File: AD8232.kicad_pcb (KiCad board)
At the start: 2 copper layers, 33 parts, among them J1 Conn_01x03, J2 Conn_01x06, J3 AudioJack3, M1 AD8232

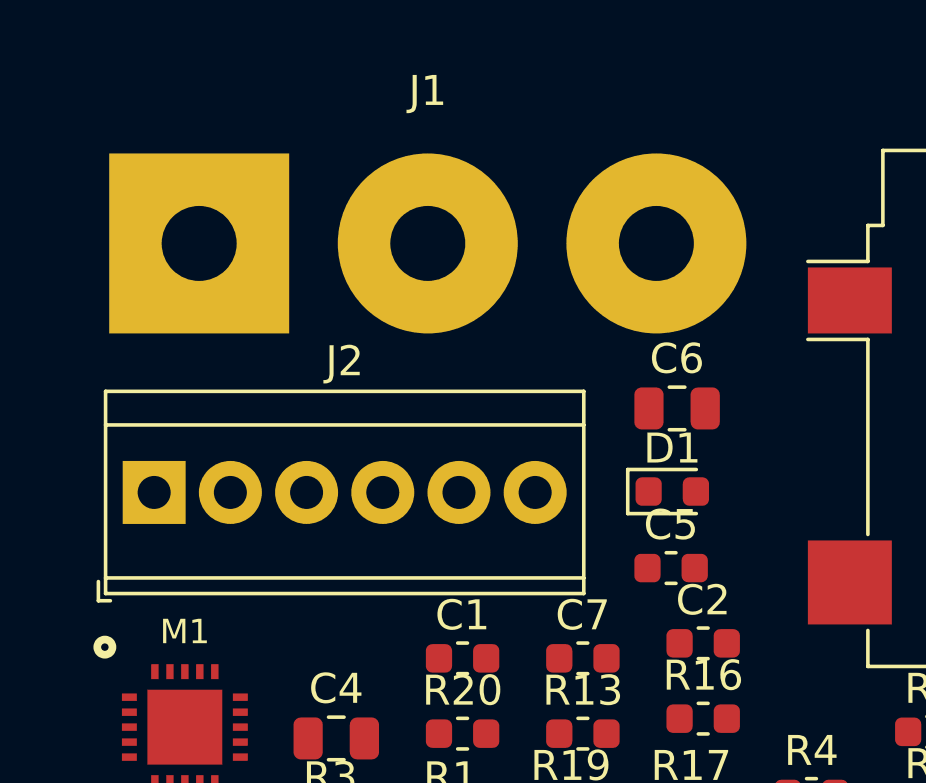
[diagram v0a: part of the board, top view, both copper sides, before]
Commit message: usar huellas de conectores 1x03 y 1x06 de SparkFun
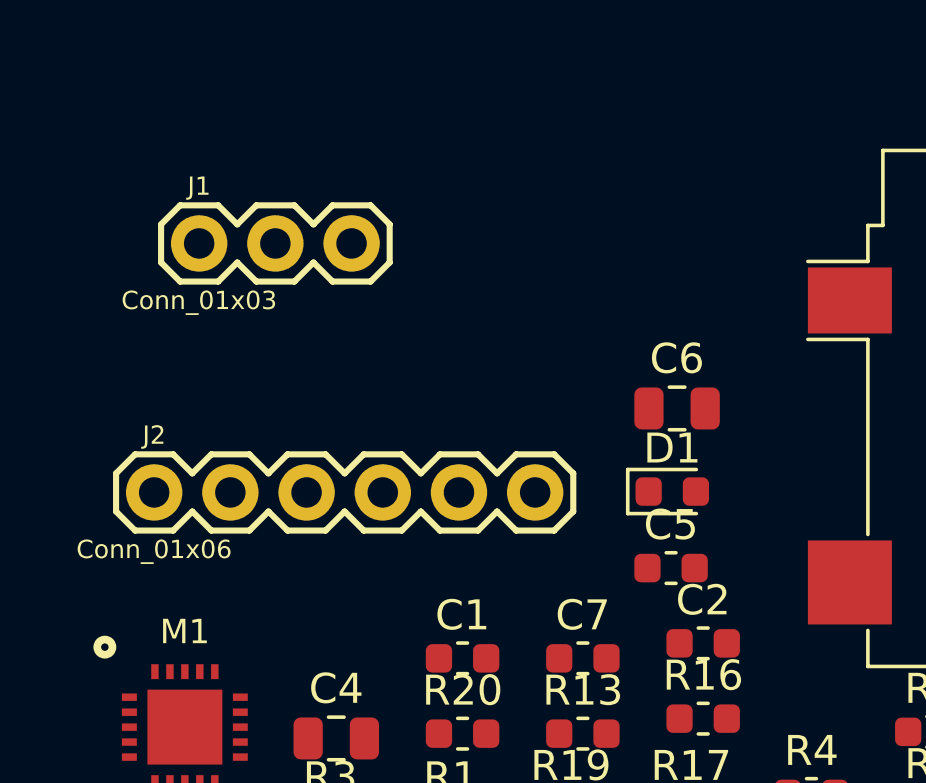
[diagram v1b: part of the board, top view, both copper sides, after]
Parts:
- J1: footprint Connector_Wire:SolderWirePad_1x03_P7.62mm_Drill2.5mm -> fp:1X03
- J2: footprint TerminalBlock_TE-Connectivity:TerminalBlock_TE_282834-6_1x06_P2.54mm_Horizontal -> fp:1X06

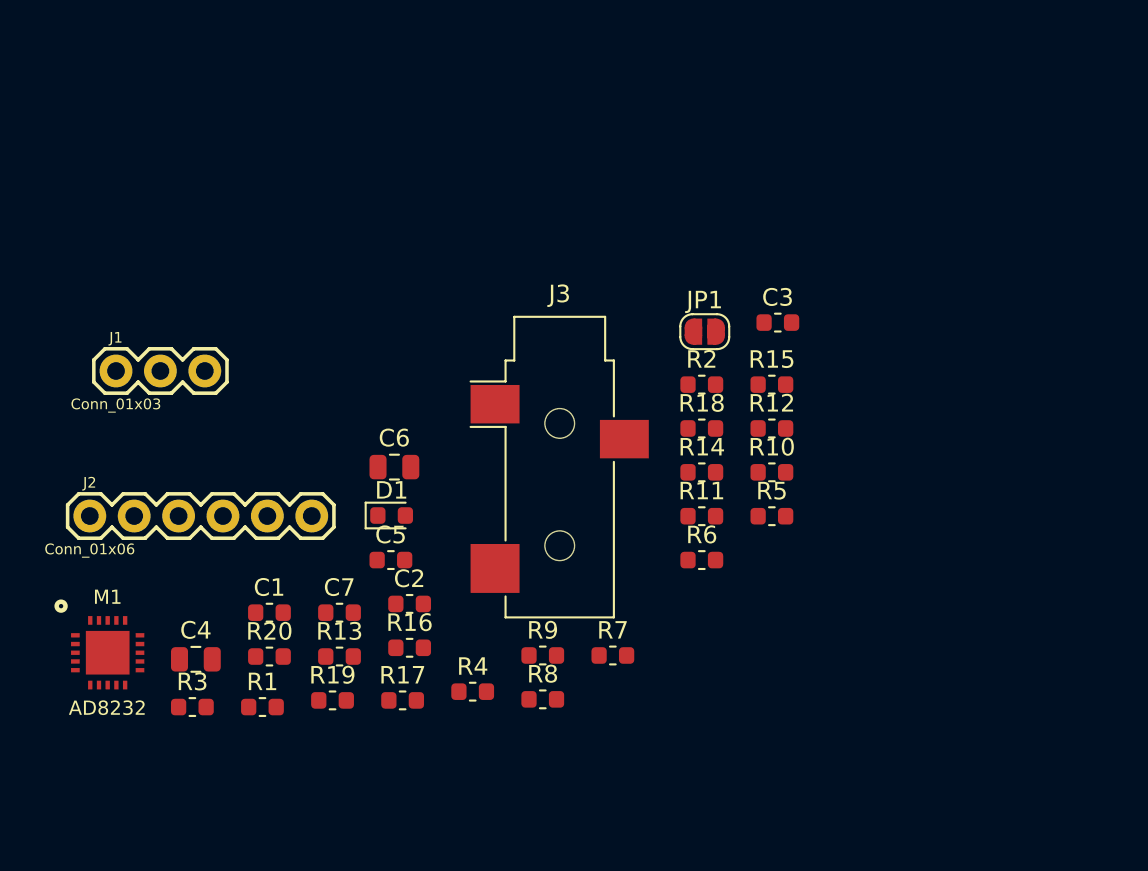
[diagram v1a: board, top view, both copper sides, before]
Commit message: primera colocacacion de componentes en el PCB
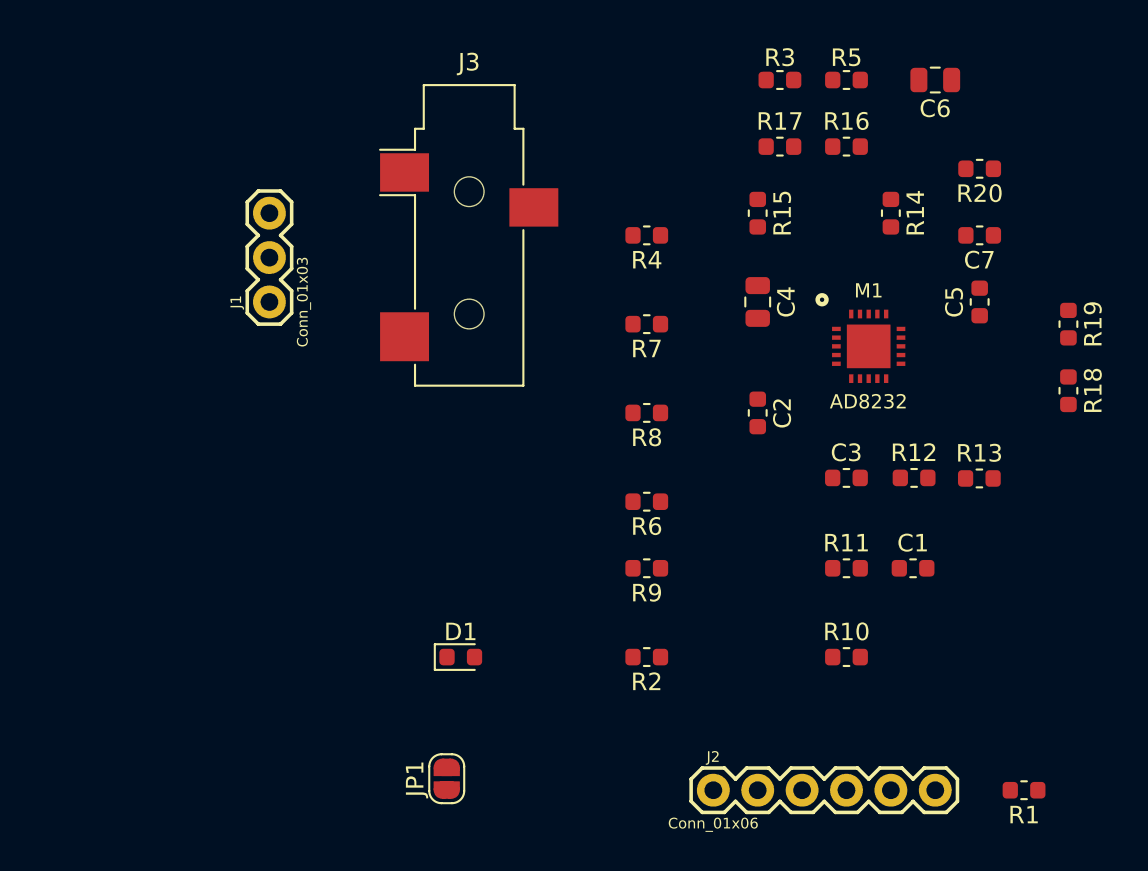
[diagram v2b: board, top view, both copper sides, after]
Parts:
- moved R20 49.3 mm to (168.9, 78.7), turned to 180 degrees
- moved R3 49.2 mm to (157.5, 73.7), turned to 180 degrees
- moved R19 47.3 mm to (174.0, 87.6), turned to 270 degrees
- moved M1 46.9 mm to (162.6, 88.9)
- moved R1 43.8 mm to (171.4, 114.3), turned to 180 degrees
- moved C7 42.5 mm to (168.9, 82.5), turned to 180 degrees
- moved J2 39.0 mm to (153.7, 114.3)
- moved R17 38.3 mm to (157.5, 77.5)
- moved C4 38.1 mm to (156.2, 86.4), turned to 270 degrees
- moved C6 38.1 mm to (166.4, 73.7), turned to 180 degrees
- moved R16 38.0 mm to (161.3, 77.5)
- moved R13 38.0 mm to (168.9, 96.5)
- moved C1 36.9 mm to (165.1, 101.6)
- moved C5 36.8 mm to (168.9, 86.4), turned to 90 degrees
- moved JP1 29.5 mm to (138.4, 113.6), turned to 90 degrees
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
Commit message: agregar pistas al PCB, excluyendo GND y REFOUT
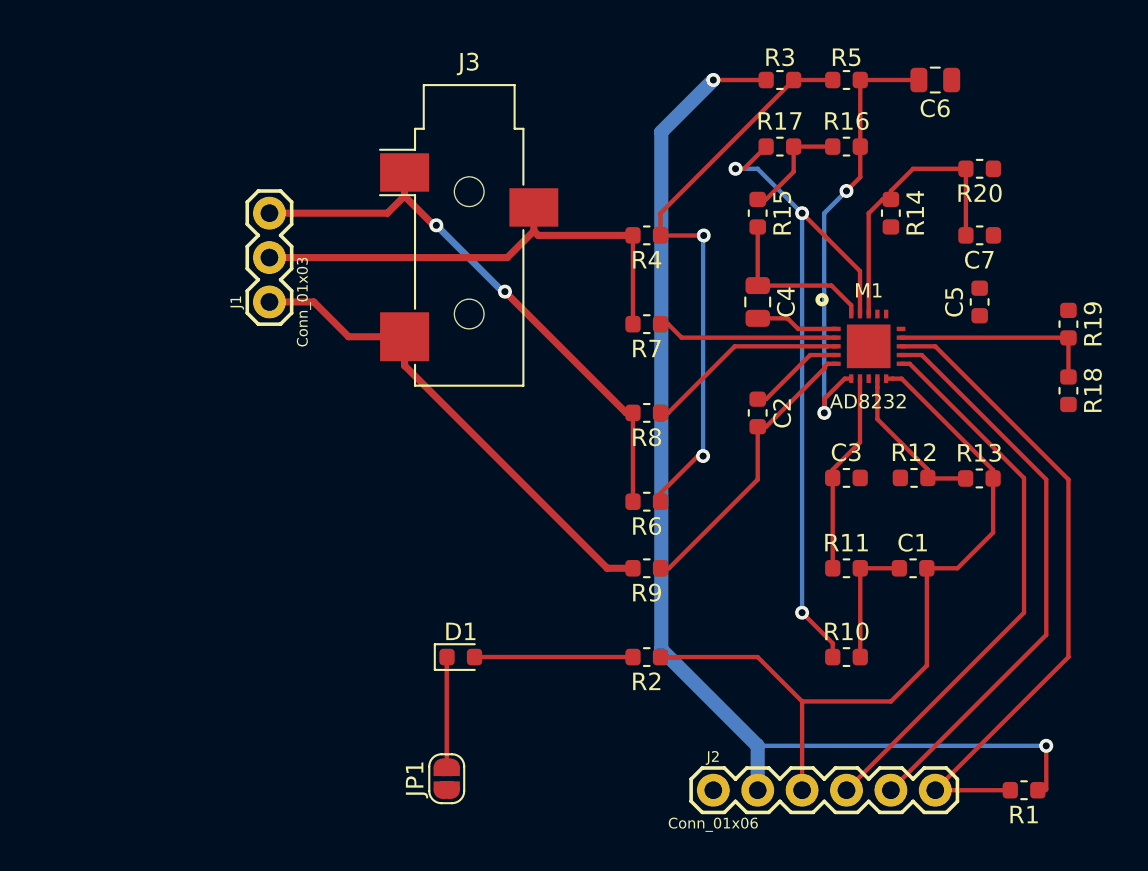
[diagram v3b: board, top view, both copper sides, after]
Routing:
- net +3V3: track 0.00 -> 66.7 mm, vias 0 -> 2
- net /SIGNAL_OUT: track 0.00 -> 44.3 mm
- net Net-(M1-Pad19): track 0.00 -> 40.4 mm, vias 0 -> 3
- net /SDN: track 0.00 -> 38.0 mm
- net Net-(R3-Pad1): track 0.00 -> 33.2 mm, vias 0 -> 2
- net /RA: track 0.00 -> 32.8 mm, vias 0 -> 2
- net /LO+: track 0.00 -> 32.7 mm
- net /LO-: track 0.00 -> 31.8 mm
- net /RL: track 0.00 -> 28.1 mm
- net /LA: track 0.00 -> 28.0 mm
- net Net-(C6-Pad2): track 0.00 -> 26.1 mm, vias 0 -> 2
- net Net-(C2-Pad2): track 0.00 -> 16.7 mm
- net Net-(C7-Pad2): track 0.00 -> 16.5 mm
- net Net-(M1-Pad14): track 0.00 -> 11.8 mm
- net Net-(M1-Pad3): track 0.00 -> 11.6 mm
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
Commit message: agregar pistas de +3.3v pendientes
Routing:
- net +3V3: track 66.7 -> 111.3 mm, vias 2 -> 5
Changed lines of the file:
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@@
     (thickness 1.6)
     (drawings 0)
-    (tracks 155)
+    (tracks 177)
     (zones 0)
     (modules 33)
@@
   (segment (start 172.675 114.3) (end 172.2375 114.3) (width 0.25) (layer F.Cu) (net 9))
   (segment (start 172.72 111.76) (end 172.72 114.255) (width 0.25) (layer F.Cu) (net 9))
+  (via (at 166.37 83.82) (size 0.8) (drill 0.4) (layers F.Cu B.Cu) (net 9))
+  (segment (start 166.173002 83.82) (end 166.37 83.82) (width 0.25) (layer B.Cu) (net 9))
+  (segment (start 153.67 73.66) (end 156.013002 73.66) (width 0.813) (layer B.Cu) (net 9))
+  (segment (start 156.013002 73.66) (end 166.173002 83.82) (width 0.813) (layer B.Cu) (net 9))
+  (segment (start 163.83 82.505) (end 163.83 82.0675) (width 0.25) (layer F.Cu) (net 9))
+  (segment (start 165.145 83.82) (end 163.83 82.505) (width 0.25) (layer F.Cu) (net 9))
+  (segment (start 166.37 83.82) (end 165.145 83.82) (width 0.25) (layer F.Cu) (net 9))
+  (segment (start 168.91 85.135) (end 168.91 85.5725) (width 0.25) (layer F.Cu) (net 9))
+  (segment (start 167.595 83.82) (end 168.91 85.135) (width 0.25) (layer F.Cu) (net 9))
+  (segment (start 166.37 83.82) (end 167.595 83.82) (width 0.25) (layer F.Cu) (net 9))
+  (via (at 173.99 85.09) (size 0.8) (drill 0.4) (layers F.Cu B.Cu) (net 9))
+  (segment (start 166.37 83.82) (end 172.72 83.82) (width 0.813) (layer B.Cu) (net 9))
+  (segment (start 172.72 83.82) (end 173.99 85.09) (width 0.813) (layer B.Cu) (net 9))
+  (segment (start 173.99 85.09) (end 173.99 86.8425) (width 0.25) (layer F.Cu) (net 9))
+  (via (at 166.37 87.098718) (size 0.8) (drill 0.4) (layers F.Cu B.Cu) (net 9))
+  (segment (start 166.37 83.82) (end 166.37 87.098718) (width 0.813) (layer B.Cu) (net 9))
+  (segment (start 164.40912 87.52732) (end 164.40912 87.90178) (width 0.25) (layer F.Cu) (net 9))
+  (segment (start 164.837722 87.098718) (end 164.40912 87.52732) (width 0.25) (layer F.Cu) (net 9))
+  (segment (start 166.37 87.098718) (end 164.837722 87.098718) (width 0.25) (layer F.Cu) (net 9))
+  (segment (start 165.7898 83.82) (end 163.05784 86.55196) (width 0.25) (layer F.Cu) (net 9))
+  (segment (start 163.05784 86.55196) (end 163.05784 87.05088) (width 0.25) (layer F.Cu) (net 9))
+  (segment (start 166.37 83.82) (end 165.7898 83.82) (width 0.25) (layer F.Cu) (net 9))
   (segment (start 165.4325 73.66) (end 162.0775 73.66) (width 0.25) (layer F.Cu) (net 11))
   (segment (start 162.0775 73.66) (end 162.0775 77.47) (width 0.25) (layer F.Cu) (net 11))

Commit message: agregar pistas de REFOUT
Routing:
- net /REFOUT: track 0.00 -> 48.3 mm, vias 0 -> 2
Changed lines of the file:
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@@
     (thickness 1.6)
     (drawings 0)
-    (tracks 177)
+    (tracks 196)
     (zones 0)
     (modules 33)
@@
   (segment (start 156.685 91.9225) (end 159.20966 89.39784) (width 0.25) (layer F.Cu) (net 4))
   (segment (start 156.21 91.9225) (end 156.685 91.9225) (width 0.25) (layer F.Cu) (net 4))
+  (via (at 170.18 73.66) (size 0.8) (drill 0.4) (layers F.Cu B.Cu) (net 5))
+  (segment (start 167.3075 73.66) (end 170.18 73.66) (width 0.25) (layer F.Cu) (net 5))
+  (via (at 163.204451 98.65646) (size 0.8) (drill 0.4) (layers F.Cu B.Cu) (net 5))
+  (segment (start 174.721509 87.139402) (end 163.204451 98.65646) (width 0.25) (layer B.Cu) (net 5))
+  (segment (start 170.18 73.66) (end 174.721509 78.201509) (width 0.25) (layer B.Cu) (net 5))
+  (segment (start 174.721509 78.201509) (end 174.721509 87.139402) (width 0.25) (layer B.Cu) (net 5))
+  (segment (start 162.074484 97.526493) (end 162.074484 96.430093) (width 0.25) (layer F.Cu) (net 5))
+  (segment (start 163.204451 98.65646) (end 162.074484 97.526493) (width 0.25) (layer F.Cu) (net 5))
+  (segment (start 164.369692 96.430093) (end 164.370714 96.429071) (width 0.25) (layer F.Cu) (net 5))
+  (segment (start 162.074484 96.430093) (end 162.56 96.52) (width 0.25) (layer F.Cu) (net 5))
+  (segment (start 164.370714 97.490197) (end 163.204451 98.65646) (width 0.25) (layer F.Cu) (net 5))
+  (segment (start 164.370714 96.429071) (end 164.370714 97.490197) (width 0.25) (layer F.Cu) (net 5))
+  (segment (start 162.56 95.055857) (end 163.284132 95.779989) (width 0.25) (layer F.Cu) (net 5))
+  (segment (start 162.56 90.74912) (end 162.56 95.055857) (width 0.25) (layer F.Cu) (net 5))
+  (segment (start 162.56 96.52) (end 163.284132 96.474084) (width 0.25) (layer F.Cu) (net 5))
+  (segment (start 163.284132 95.779989) (end 163.284132 96.474084) (width 0.25) (layer F.Cu) (net 5))
+  (segment (start 163.284132 96.474084) (end 164.369692 96.430093) (width 0.25) (layer F.Cu) (net 5))
   (segment (start 162.06216 91.24804) (end 162.06216 90.74912) (width 0.25) (layer F.Cu) (net 6))
   (segment (start 162.06216 94.392417) (end 162.06216 91.24804) (width 0.25) (layer F.Cu) (net 6))
@@
   (segment (start 167.595 83.82) (end 168.91 85.135) (width 0.25) (layer F.Cu) (net 9))
   (segment (start 166.37 83.82) (end 167.595 83.82) (width 0.25) (layer F.Cu) (net 9))
-  (via (at 173.99 85.09) (size 0.8) (drill 0.4) (layers F.Cu B.Cu) (net 9))
   (segment (start 166.37 83.82) (end 172.72 83.82) (width 0.813) (layer B.Cu) (net 9))
-  (segment (start 172.72 83.82) (end 173.99 85.09) (width 0.813) (layer B.Cu) (net 9))
-  (segment (start 173.99 85.09) (end 173.99 86.8425) (width 0.25) (layer F.Cu) (net 9))
   (via (at 166.37 87.098718) (size 0.8) (drill 0.4) (layers F.Cu B.Cu) (net 9))
   (segment (start 166.37 83.82) (end 166.37 87.098718) (width 0.813) (layer B.Cu) (net 9))
@@
   (segment (start 163.05784 86.55196) (end 163.05784 87.05088) (width 0.25) (layer F.Cu) (net 9))
   (segment (start 166.37 83.82) (end 165.7898 83.82) (width 0.25) (layer F.Cu) (net 9))
+  (segment (start 172.72 83.82) (end 172.72 83.82) (width 0.813) (layer B.Cu) (net 9))
+  (via (at 172.72 83.82) (size 0.8) (drill 0.4) (layers F.Cu B.Cu) (net 9))
+  (segment (start 173.515 86.8425) (end 173.99 86.8425) (width 0.25) (layer F.Cu) (net 9))
+  (segment (start 172.72 86.0475) (end 173.515 86.8425) (width 0.25) (layer F.Cu) (net 9))
+  (segment (start 172.72 83.82) (end 172.72 86.0475) (width 0.25) (layer F.Cu) (net 9))
   (segment (start 165.4325 73.66) (end 162.0775 73.66) (width 0.25) (layer F.Cu) (net 11))
   (segment (start 162.0775 73.66) (end 162.0775 77.47) (width 0.25) (layer F.Cu) (net 11))
